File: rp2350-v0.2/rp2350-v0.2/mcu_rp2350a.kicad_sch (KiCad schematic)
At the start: 31 parts, among them SW4 SW_Push, U1 RP2350A-QFN60, Y1 ABM8-272-T3, Y2 SIT1533AI-H4-DCC-32.768E

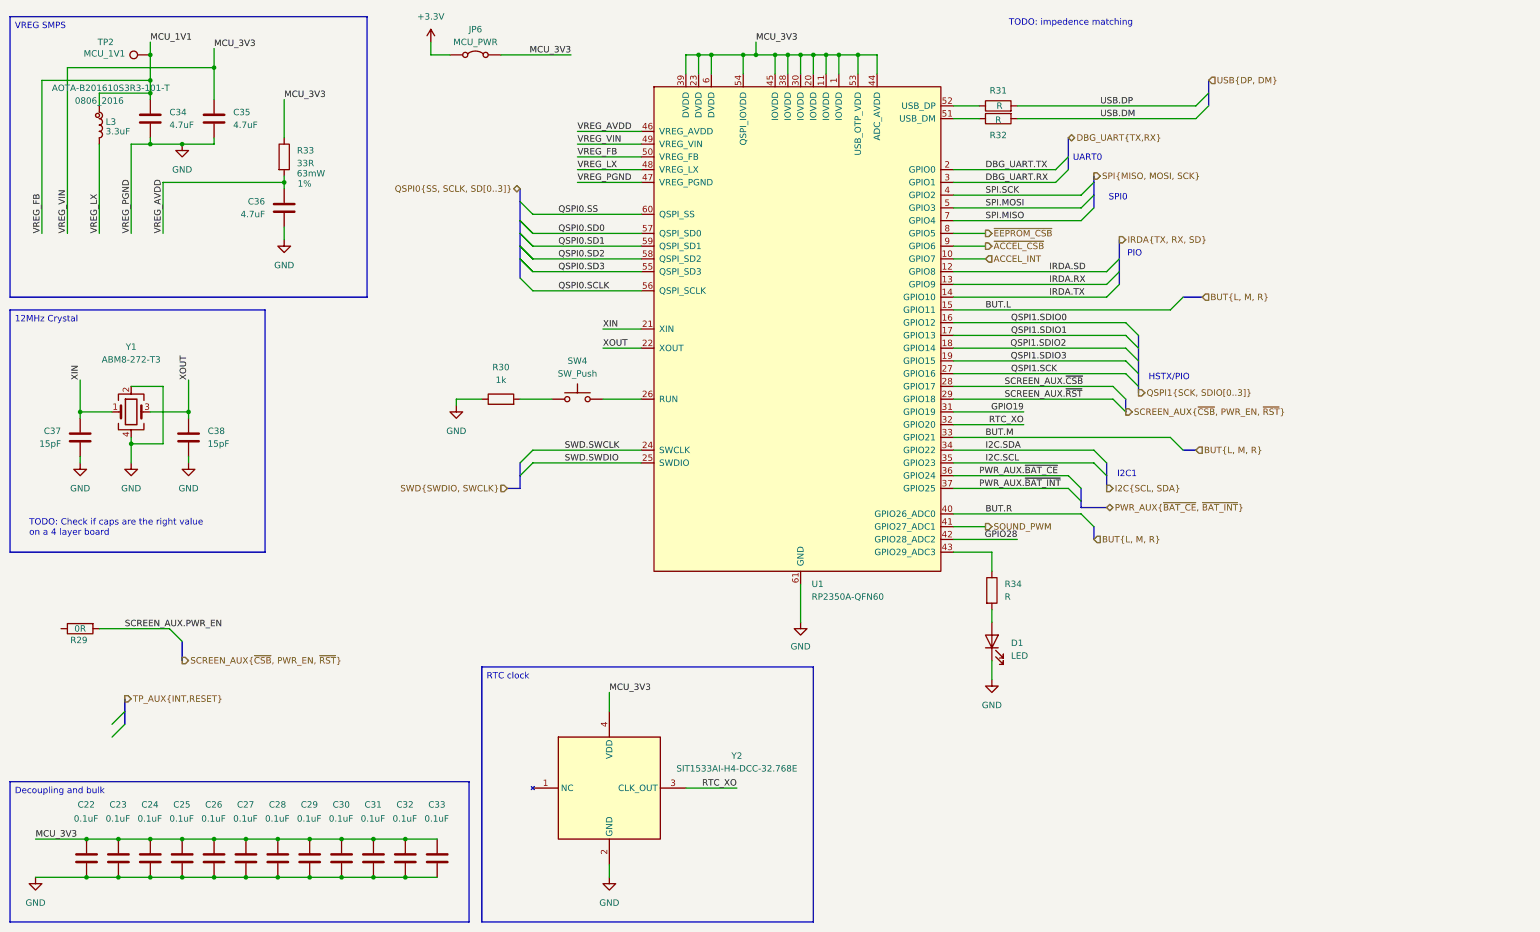
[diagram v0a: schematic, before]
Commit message: v0.2: schematic draft 1 done
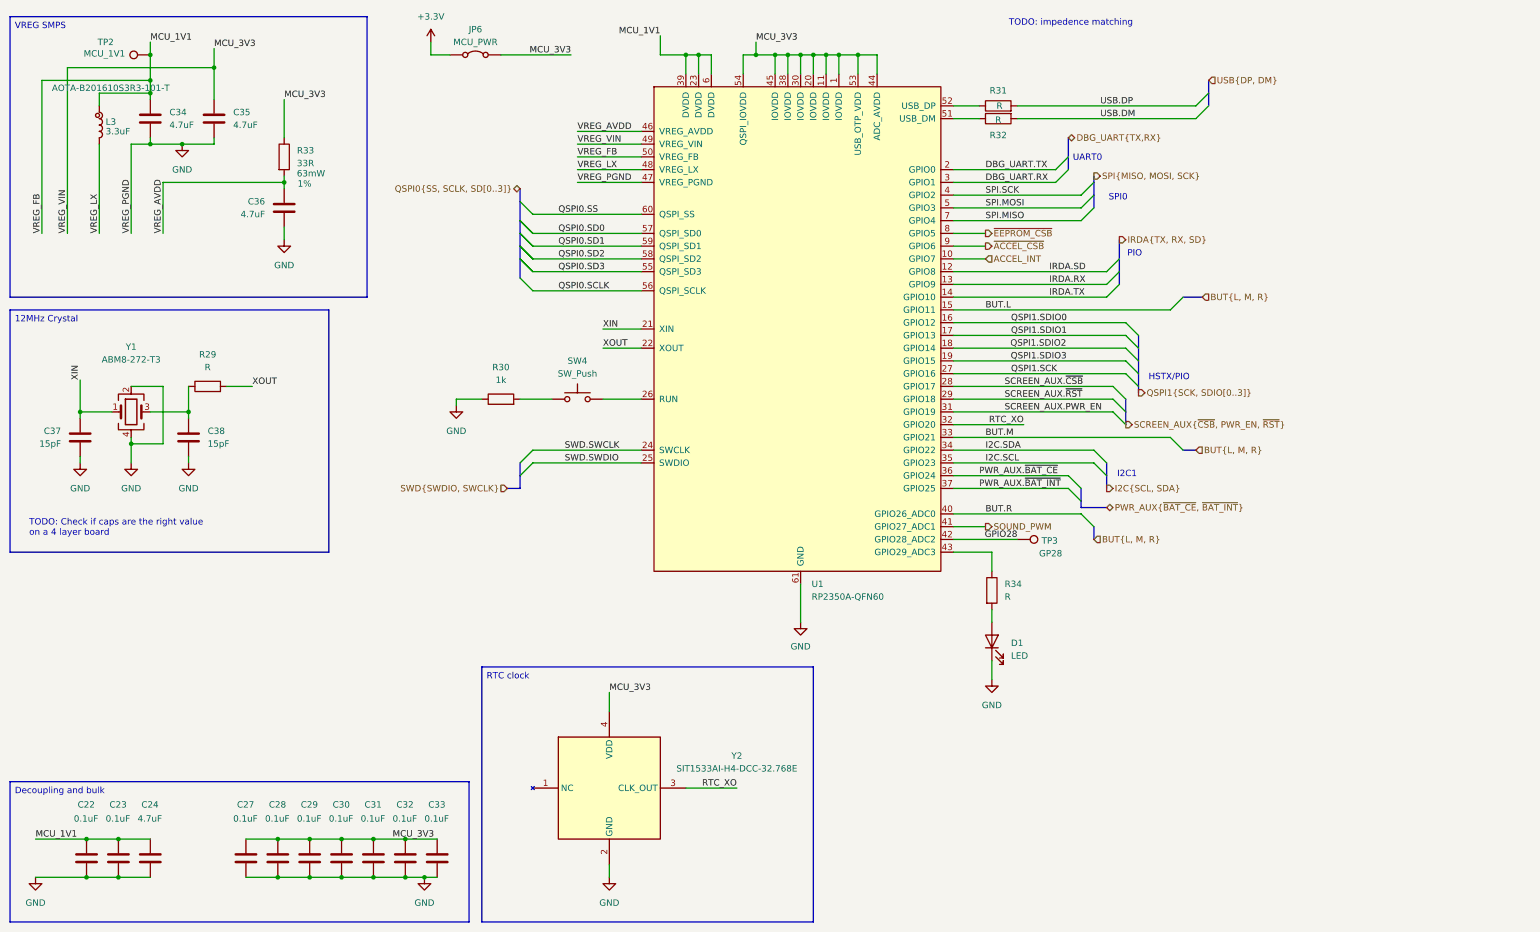
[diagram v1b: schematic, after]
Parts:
- removed C25, C26: 0.1uF, Capacitor_SMD:C_0402_1005Metric, symbol Device:C
- added TP3: GP28, TestPoint:TestPoint_Pad_2.5x2.5mm, symbol Connector:TestPoint
- C24: value 0.1uF -> 4.7uF
- JP6: footprint (none) -> CustomFootprints:BridgedJumper_P2.54mm
- L3: footprint (none) -> CustomFootprints:L_0805_2016Metric
- R29: value 0R -> R; footprint Resistor_SMD:R_0603_1608Metric -> Resistor_SMD:R_0402_1005Metric
- TP2: footprint (none) -> TestPoint:TestPoint_Pad_2.5x2.5mm
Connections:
- net GPIO19 is gone; now on net SCREEN_AUX.PWR_EN: U1.31 (GPIO19)
- net GPIO28: now also TP3.1
- net MCU_1V1: now also C22.1, C23.1, C24.1, U1.23 (DVDD), U1.39 (DVDD), U1.6 (DVDD)
- net MCU_3V3: no longer C22.1, C23.1, C24.1, U1.23 (DVDD), U1.39 (DVDD), U1.6 (DVDD)
- net SCREEN_AUX.PWR_EN: no longer R29.2
- net XOUT: now also R29.2; no longer C38.1, Y1.3
- net at R29.1: now also C38.1, Y1.3

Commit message: v0.2: loads of progress now gonna change it all up again
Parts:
- R34: value R -> 1k
- TP3: value GP28 -> GP26
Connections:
- net BUT.L: now also U1.27 (GPIO16); no longer U1.15 (GPIO11)
- net BUT.R: now also U1.41 (GPIO27_ADC1); no longer U1.40 (GPIO26_ADC0)
- net IRDA.RX: now also U1.18 (GPIO14); no longer U1.13 (GPIO9)
- net IRDA.SD: now also U1.17 (GPIO13); no longer U1.12 (GPIO8)
- net IRDA.TX: now also U1.19 (GPIO15); no longer U1.14 (GPIO10)
- net PWR_AUX.~{BAT_CE}: now also U1.43 (GPIO29_ADC3); no longer U1.36 (GPIO24)
- net PWR_AUX.~{BAT_INT}: now also U1.42 (GPIO28_ADC2); no longer U1.37 (GPIO25)
- net QSPI1.SCK: now also U1.12 (GPIO8); no longer U1.27 (GPIO16)
- net QSPI1.SDIO1: now also U1.15 (GPIO11); no longer U1.17 (GPIO13)
- net QSPI1.SDIO2: now also U1.14 (GPIO10); no longer U1.18 (GPIO14)
- net QSPI1.SDIO3: now also U1.13 (GPIO9); no longer U1.19 (GPIO15)
- net SOUND_PWM: now also U1.36 (GPIO24); no longer U1.41 (GPIO27_ADC1)
- net GPIO25: now reaches R34.1
- net GPIO25: now also U1.37 (GPIO25); no longer U1.43 (GPIO29_ADC3)
- net GPIO28 renamed GPIO26
- net GPIO26: now also U1.40 (GPIO26_ADC0); no longer U1.42 (GPIO28_ADC2)
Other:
- note added: "PIO. Note decreasing numbers, so need to swap nibbles in software."
- note removed: "HSTX/PIO"
- moved on the sheet: D1, R34, TP3

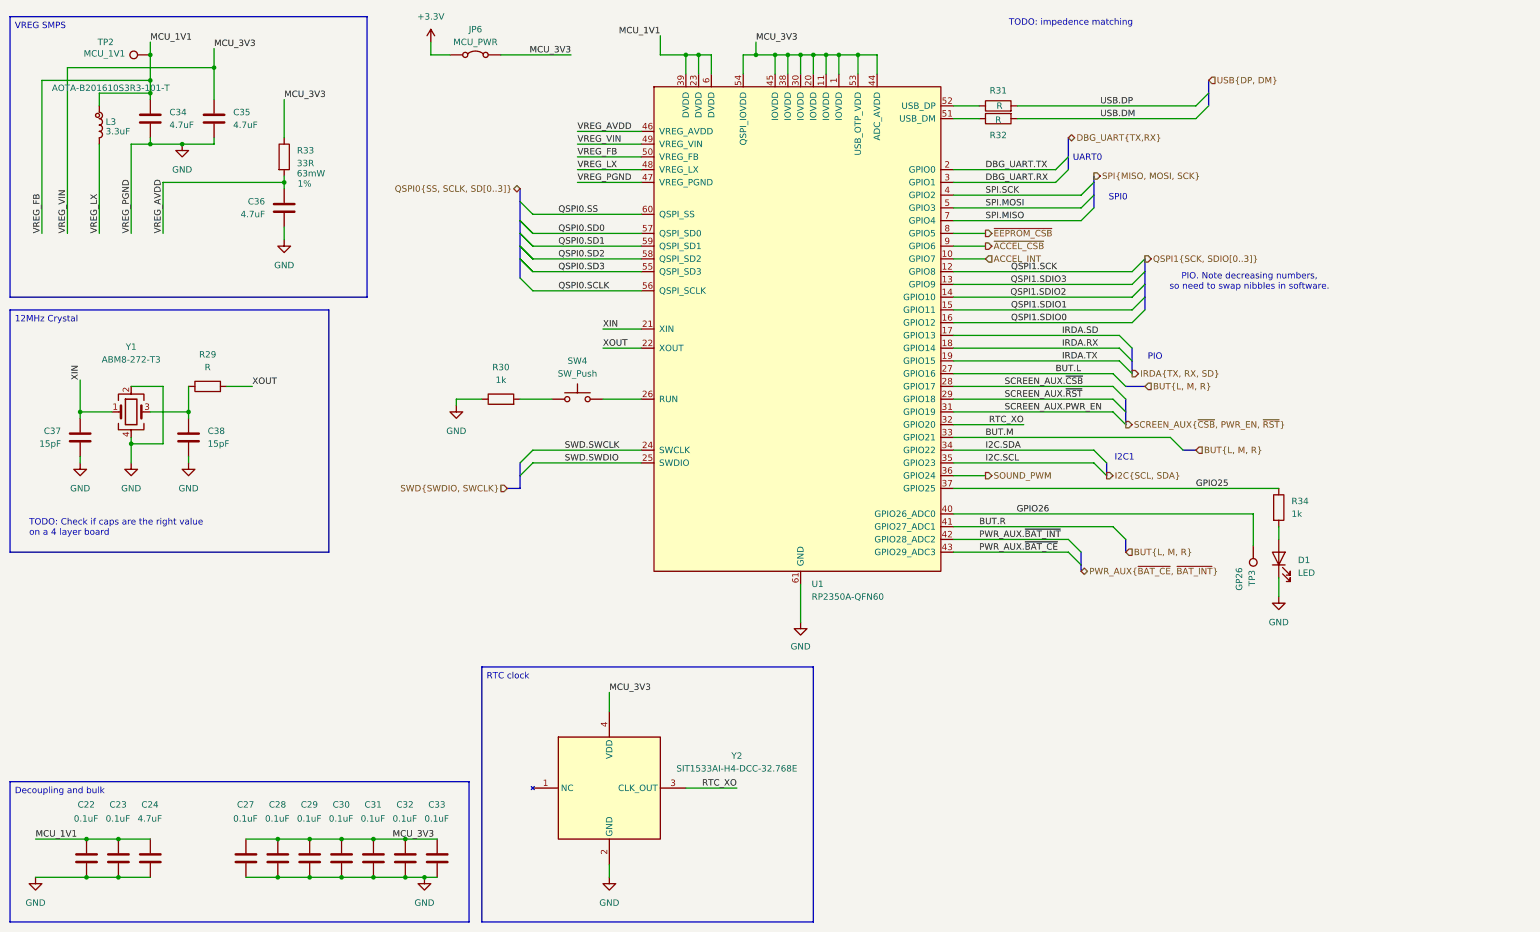
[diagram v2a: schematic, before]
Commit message: v0.2: more progress on routing, nearly done
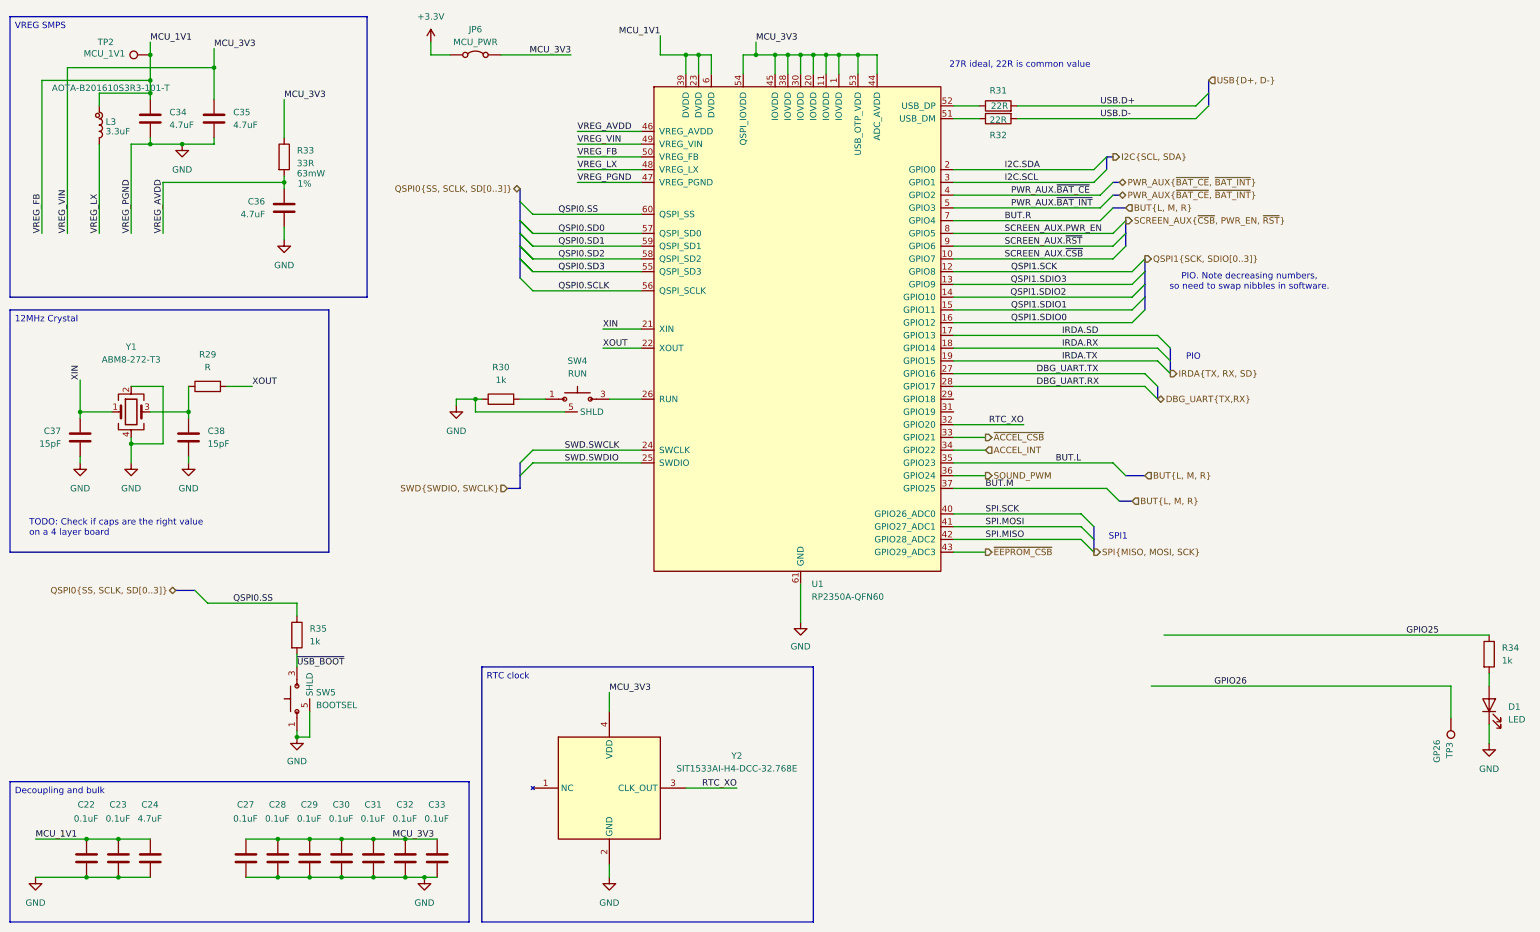
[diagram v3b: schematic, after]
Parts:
- added R35: 1k, Resistor_SMD:R_0402_1005Metric, symbol Device:R
- added SW5: BOOTSEL, CustomFootprints:WS_TASV_435151014824, symbol CustomSymbols:WS_TASV_435151014824
- R31, R32: value R -> 22R
- SW4: value SW_Push -> RUN; footprint Button_Switch_SMD:SW_SPST_Omron_B3FS-101xP -> CustomFootprints:WS_TASV_435151014824; symbol Switch:SW_Push -> CustomSymbols:WS_TASV_435151014824
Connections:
- net ACCEL_INT: now also U1.34 (GPIO22); no longer U1.10 (GPIO7)
- net BUT.L: now also U1.35 (GPIO23); no longer U1.27 (GPIO16)
- net BUT.M: now also U1.37 (GPIO25); no longer U1.33 (GPIO21)
- net BUT.R: now also U1.7 (GPIO4); no longer U1.41 (GPIO27_ADC1)
- net DBG_UART.RX: now also U1.28 (GPIO17); no longer U1.3 (GPIO1)
- net DBG_UART.TX: now also U1.27 (GPIO16); no longer U1.2 (GPIO0)
- net GND: now also SW4.5 (SHLD), SW4.6 (SHLD), SW5.1, SW5.2, SW5.5 (SHLD), SW5.6 (SHLD)
- net GPIO25: no longer U1.37 (GPIO25)
- net GPIO26: no longer U1.40 (GPIO26_ADC0)
- net I2C.SCL: now also U1.3 (GPIO1); no longer U1.35 (GPIO23)
- net I2C.SDA: now also U1.2 (GPIO0); no longer U1.34 (GPIO22)
- net PWR_AUX.~{BAT_CE}: now also U1.4 (GPIO2); no longer U1.43 (GPIO29_ADC3)
- net PWR_AUX.~{BAT_INT}: now also U1.5 (GPIO3); no longer U1.42 (GPIO28_ADC2)
- net QSPI0.SS: now also R35.1
- net SCREEN_AUX.PWR_EN: now also U1.8 (GPIO5); no longer U1.31 (GPIO19)
- net SCREEN_AUX.~{CSB}: now also U1.10 (GPIO7); no longer U1.28 (GPIO17)
- net SCREEN_AUX.~{RST}: now also U1.9 (GPIO6); no longer U1.29 (GPIO18)
- net SPI.MISO: now also U1.42 (GPIO28_ADC2); no longer U1.7 (GPIO4)
- net SPI.MOSI: now also U1.41 (GPIO27_ADC1); no longer U1.5 (GPIO3)
- net SPI.SCK: now also U1.40 (GPIO26_ADC0); no longer U1.4 (GPIO2)
- net ~{ACCEL_CSB}: now also U1.33 (GPIO21); no longer U1.9 (GPIO6)
- net ~{EEPROM_CSB}: now also U1.43 (GPIO29_ADC3); no longer U1.8 (GPIO5)
- net at R30.2, SW4.1: now also SW4.2
- net at U1.26 (RUN): now also SW4.3, SW4.4; no longer SW4.2
- net USB.DM renamed USB.D-
- net USB.DP renamed USB.D+
- new net ~{USB_BOOT}: R35.2, SW5.3, SW5.4
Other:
- note added: "27R ideal, 22R is common value"
- note added: "SPI1"
- note removed: "I2C1"
- note removed: "SPI0"
- note removed: "TODO: impedence matching"
- note removed: "UART0"
- moved on the sheet: D1, R34, TP3

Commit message: v0.2: routing done, nearly ready for prod
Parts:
- added TP9: GP18, TestPoint:TestPoint_Pad_2.5x2.5mm, symbol Connector:TestPoint
- D1: value LED -> USER_LED
- TP3: value GP26 -> GP19
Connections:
- net GPIO25 is gone; now on net GPIO18: R34.1
- net GPIO26 is gone; now on net GPIO19: TP3.1
- net GPIO18: now reaches U1.29 (GPIO18)
- net GPIO18: now also TP9.1
- net GPIO19: now reaches U1.31 (GPIO19)
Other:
- moved on the sheet: D1, R34, TP3
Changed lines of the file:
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@@
 	)
 	(junction
+		(at 267.97 92.71)
+		(diameter 0)
+		(color 0 0 0 0)
+	)
+	(junction
 		(at 107.95 91.44)
 		(diameter 0)
@@
 	(wire
 		(pts
-			(xy 302.26 148.59) (xy 302.26 154.94)
+			(xy 262.89 93.98) (xy 262.89 100.33)
 		)
 		(stroke
@@
 	(wire
 		(pts
-			(xy 245.11 138.43) (xy 309.88 138.43)
+			(xy 212.09 92.71) (xy 267.97 92.71)
 		)
 		(stroke
@@
 	(wire
 		(pts
+			(xy 212.09 91.44) (xy 212.09 92.71)
+		)
+		(stroke
+			(width 0)
+			(type default)
+		)
+	)
+	(wire
+		(pts
 			(xy 203.2 66.04) (xy 238.76 66.04)
 		)
@@
 	(wire
 		(pts
+			(xy 276.86 92.71) (xy 276.86 95.25)
+		)
+		(stroke
+			(width 0)
+			(type default)
+		)
+	)
+	(wire
+		(pts
 			(xy 68.58 186.69) (xy 74.93 186.69)
 		)
@@
 	(wire
 		(pts
-			(xy 242.57 148.59) (xy 302.26 148.59)
+			(xy 203.2 93.98) (xy 262.89 93.98)
 		)
 		(stroke
@@
 	(wire
 		(pts
-			(xy 309.88 146.05) (xy 309.88 148.59)
+			(xy 276.86 102.87) (xy 276.86 105.41)
 		)
 		(stroke
@@
 	(wire
 		(pts
+			(xy 203.2 91.44) (xy 212.09 91.44)
+		)
+		(stroke
+			(width 0)
+			(type default)
+		)
+	)
+	(wire
+		(pts
 			(xy 33.02 30.48) (xy 43.18 30.48)
 		)
@@
 	(wire
 		(pts
-			(xy 309.88 156.21) (xy 309.88 160.02)
+			(xy 276.86 113.03) (xy 276.86 116.84)
 		)
 		(stroke
@@
 	(wire
 		(pts
+			(xy 267.97 92.71) (xy 276.86 92.71)
+		)
+		(stroke
+			(width 0)
+			(type default)
+		)
+	)
+	(wire
+		(pts
 			(xy 43.18 22.86) (xy 43.18 27.94)
 		)
@@
 		)
 	)
-	(label "GPIO25"
-		(at 293.37 138.43 0)
+	(label "GPIO18"
+		(at 264.16 92.71 0)
 		(effects
 			(font
@@
 		)
 	)
-	(label "GPIO26"
-		(at 261.62 148.59 180)
+	(label "GPIO19"
+		(at 222.25 93.98 180)
 		(effects
 			(font
@@
 	(symbol
 		(lib_id "Device:LED")
-		(at 309.88 152.4 90)
+		(at 276.86 109.22 90)
 		(unit 1)
 		(exclude_from_sim no)
@@
 		(fields_autoplaced yes)
 		(property "Reference" "D1"
-			(at 313.69 152.7174 90)
+			(at 280.67 109.5374 90)
 			(effects
 				(font
@@
 			)
 		)
-		(property "Value" "LED"
-			(at 313.69 155.2574 90)
+		(property "Value" "USER_LED"
+			(at 280.67 112.0774 90)
 			(effects
 				(font
@@
 		)
 		(property "Footprint" "LED_SMD:LED_0402_1005Metric"
-			(at 309.88 152.4 0)
+			(at 276.86 109.22 0)
 			(effects
 				(font
@@
 		)
 		(property "Datasheet" "~"
-			(at 309.88 152.4 0)
+			(at 276.86 109.22 0)
 			(effects
 				(font
@@
 		)
 		(property "Description" "Light emitting diode"
-			(at 309.88 152.4 0)
+			(at 276.86 109.22 0)
 			(effects
 				(font
@@
 		)
 		(property "Sim.Pins" "1=K 2=A"
-			(at 309.88 152.4 0)
+			(at 276.86 109.22 0)
 			(effects
 				(font
@@
 	)
 	(symbol
+		(lib_id "Connector:TestPoint")
+		(at 267.97 92.71 180)
+		(unit 1)
+		(exclude_from_sim no)
+		(in_bom yes)
+		(on_board yes)
+		(dnp no)
+		(fields_autoplaced yes)
+		(property "Reference" "TP9"
+			(at 270.51 94.7419 0)
+			(effects
+				(font
+					(size 1.27 1.27)
+				)
+				(justify right)
+			)
+		)
+		(property "Value" "GP18"
+			(at 270.51 97.2819 0)
+			(effects
+				(font
+					(size 1.27 1.27)
+				)
+				(justify right)
+			)
+		)
+		(property "Footprint" "TestPoint:TestPoint_Pad_2.5x2.5mm"
+			(at 262.89 92.71 0)
+			(effects
+				(font
+					(size 1.27 1.27)
+				)
+				(hide yes)
+			)
+		)
+		(property "Datasheet" "~"
+			(at 262.89 92.71 0)
+			(effects
+				(font
+					(size 1.27 1.27)
+				)
+				(hide yes)
+			)
+		)
+		(property "Description" "test point"
+			(at 267.97 92.71 0)
+			(effects
+				(font
+					(size 1.27 1.27)
+				)
+				(hide yes)
+			)
+		)
+		(pin "1"
+		)
+		(instances
+			(project ""
+				(path "/5cbb45d4-7f83-48dd-a53b-5c75c7d1d827/43898cce-4488-4636-8fe4-d95251b1544a"
+					(reference "TP9")
+					(unit 1)
+				)
+			)
+		)
+	)
+	(symbol
 		(lib_id "rp2350a-qfn60:RP2350A-QFN60")
 		(at 172.72 73.66 0)
@@
 	(symbol
 		(lib_id "Device:R")
-		(at 309.88 142.24 0)
+		(at 276.86 99.06 0)
 		(unit 1)
 		(exclude_from_sim no)
@@
 		(fields_autoplaced yes)
 		(property "Reference" "R34"
-			(at 312.42 140.9699 0)
+			(at 279.4 97.7899 0)
 			(effects
 				(font
@@
 		)
 		(property "Value" "1k"
-			(at 312.42 143.5099 0)
+			(at 279.4 100.3299 0)
 			(effects
 				(font
@@
 		)
 		(property "Footprint" "Resistor_SMD:R_0402_1005Metric"
-			(at 308.102 142.24 90)
+			(at 275.082 99.06 90)
 			(effects
 				(font
@@
 		)
 		(property "Datasheet" "~"
-			(at 309.88 142.24 0)
+			(at 276.86 99.06 0)
 			(effects
 				(font
@@
 		)
 		(property "Description" "Resistor"
-			(at 309.88 142.24 0)
+			(at 276.86 99.06 0)
 			(effects
 				(font
@@
 	(symbol
 		(lib_id "power:GND")
-		(at 309.88 160.02 0)
+		(at 276.86 116.84 0)
 		(unit 1)
 		(exclude_from_sim no)
@@
 		(fields_autoplaced yes)
 		(property "Reference" "#PWR072"
-			(at 309.88 166.37 0)
+			(at 276.86 123.19 0)
 			(effects
 				(font
@@
 		)
 		(property "Value" "GND"
-			(at 309.88 165.1 0)
+			(at 276.86 121.92 0)
 			(effects
 				(font
@@
 		)
 		(property "Footprint" ""
-			(at 309.88 160.02 0)
+			(at 276.86 116.84 0)
 			(effects
 				(font
@@
 		)
 		(property "Datasheet" ""
-			(at 309.88 160.02 0)
+			(at 276.86 116.84 0)
 			(effects
 				(font
@@
 		)
 		(property "Description" "Power symbol creates a global label with name \"GND\" , ground"
-			(at 309.88 160.02 0)
+			(at 276.86 116.84 0)
 			(effects
 				(font
@@
 	(symbol
 		(lib_id "Connector:TestPoint")
-		(at 302.26 154.94 180)
+		(at 262.89 100.33 180)
 		(unit 1)
 		(exclude_from_sim no)
@@
 		(dnp no)
 		(property "Reference" "TP3"
-			(at 302.006 159.766 90)
+			(at 262.636 105.156 90)
 			(effects
 				(font
@@
 			)
 		)
-		(property "Value" "GP26"
-			(at 299.466 159.258 90)
+		(property "Value" "GP19"
+			(at 260.096 104.648 90)
 			(effects
 				(font
@@
 		)
 		(property "Footprint" "TestPoint:TestPoint_Pad_2.5x2.5mm"
-			(at 297.18 154.94 0)
+			(at 257.81 100.33 0)
 			(effects
 				(font
@@
 		)
 		(property "Datasheet" "~"
-			(at 297.18 154.94 0)
+			(at 257.81 100.33 0)
 			(effects
 				(font
@@
 		)
 		(property "Description" "test point"
-			(at 302.26 154.94 0)
+			(at 262.89 100.33 0)
 			(effects
 				(font
